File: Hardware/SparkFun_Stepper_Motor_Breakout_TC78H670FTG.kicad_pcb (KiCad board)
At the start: 4 copper layers, 15.2 x 20.3 mm, 45 parts, among them J1 Conn_01x08, J2 Conn_01x08, U1 TC78H670FTG

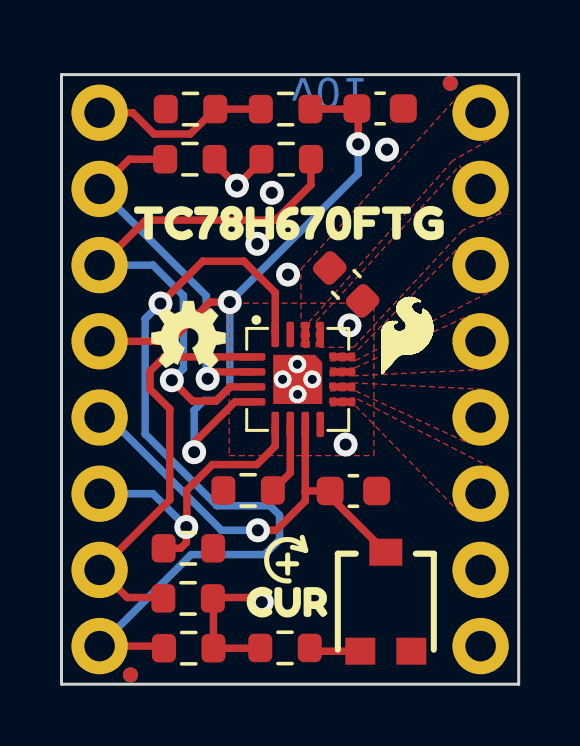
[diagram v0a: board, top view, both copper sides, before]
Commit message: more tweaks for DRC
-inner layer zone properties min width changed from .3 to .2 to allow flow and more thermal spokes on 3v3 header
-DRC exclusions for fiducials
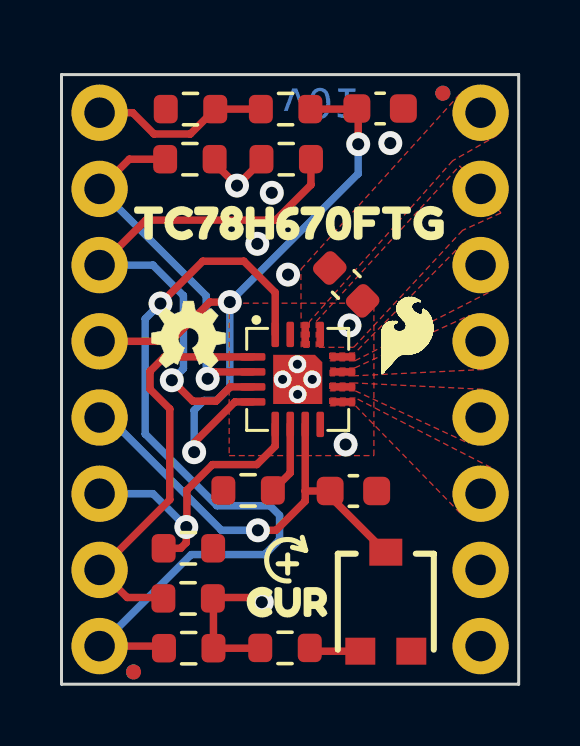
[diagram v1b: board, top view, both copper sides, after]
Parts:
- moved FID1 0.41 mm to (147.3, 94.6)
- moved FID2 0.41 mm to (147.3, 94.6)
- moved FID4 0.14 mm to (137.0, 113.9)
- moved FID3 0.14 mm to (137.0, 113.9)
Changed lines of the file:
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@@
     (property "Sheetfile" "SparkFun_Stepper_Motor_Carrier_TC78H670FTG.kicad_sch")
     (property "Sheetname" "")
-    (attr smd)
+    (attr smd allow_soldermask_bridges)
     (fp_text reference "U1" (at 0.75 -1.58 unlocked) (layer "F.Fab")
         (effects (font (size 1 1) (thickness 0.1)))
@@
   )
   (footprint "SparkFun-Aesthetic:Fiducial_0.5mm_Mask1mm" (layer "F.Cu")
-    (at 136.92 113.99)
+    (at 137.021639 113.891825)
     (descr "Circular Fiducial, 0.5mm bare copper, 1mm soldermask opening (Level C)")
     (tags "fiducial")
@@
   )
   (footprint "SparkFun-Aesthetic:Fiducial_0.5mm_Mask1mm" (layer "F.Cu")
-    (at 147.58 94.27)
+    (at 147.331908 94.601097)
     (descr "Circular Fiducial, 0.5mm bare copper, 1mm soldermask opening (Level C)")
     (tags "fiducial")
@@
   )
   (footprint "SparkFun-Aesthetic:Fiducial_0.5mm_Mask1mm" (layer "B.Cu")
-    (at 147.58 94.27 180)
+    (at 147.331908 94.599043 180)
     (descr "Circular Fiducial, 0.5mm bare copper, 1mm soldermask opening (Level C)")
     (tags "fiducial")
@@
   )
   (footprint "SparkFun-Aesthetic:Fiducial_0.5mm_Mask1mm" (layer "B.Cu")
-    (at 136.92 113.99 180)
+    (at 137.019585 113.89097 180)
     (descr "Circular Fiducial, 0.5mm bare copper, 1mm soldermask opening (Level C)")
     (tags "fiducial")
@@
   (gr_rect (start 134.62 93.98) (end 149.86 114.3)
     (stroke (width 0.1) (type default)) (fill none) (layer "Edge.Cuts"))
-  (gr_text "v01" (at 142.261552 93.973312 180) (layer "B.Cu")
+  (gr_text "v01" (at 141.988553 94.318209 180) (layer "B.Cu")
     (effects (font (size 1 1) (thickness 0.15)) (justify left bottom mirror))
   )
@@
   (via (at 141.296656 111.566922) (size 0.8) (drill 0.4) (layers "F.Cu" "B.Cu") (free) (net 8))
   (via (at 140.47 97.68) (size 0.8) (drill 0.4) (layers "F.Cu" "B.Cu") (free) (net 8))
-  (via (at 145.47 96.48) (size 0.8) (drill 0.4) (layers "F.Cu" "B.Cu") (net 13))
+  (via (at 145.579788 96.263383) (size 0.8) (drill 0.4) (layers "F.Cu" "B.Cu") (net 13))
   (via (at 141.1465 99.621194) (size 0.8) (drill 0.4) (layers "F.Cu" "B.Cu") (net 13))
   (via (at 141.99 104.14) (size 0.6) (drill 0.3) (layers "F.Cu" "B.Cu") (net 13))
@@
     (priority 6)
     (connect_pads (clearance 0.2032))
-    (min_thickness 0.3) (filled_areas_thickness no)
+    (min_thickness 0.2) (filled_areas_thickness no)
     (fill yes (thermal_gap 0.2032) (thermal_bridge_width 0.3))
     (polygon

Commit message: ordering instructions
Inner copper weight
Material: TG135
Four layer stack-up
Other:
- board text added: "0.5oz Inner Layers"
- board text added: "2oz Outer Layers"
- board text added: "JLC7628 Stackup"
- board text added: "Material: TG135-140"
- board text removed: "Copper weight: 2oz"
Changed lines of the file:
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@@
     (40 "Dwgs.User" user "User.Drawings")
     (41 "Cmts.User" user "User.Comments")
-    (42 "Eco1.User" user "Dimensions")
+    (42 "Eco1.User" user "Measures")
     (43 "Eco2.User" user "User.Eco2")
     (44 "Edge.Cuts" user)
@@
     (effects (font (size 2 2) (thickness 0.15)) (justify left bottom))
   )
+  (gr_text "JLC7628 Stackup" (at 170.18 88.9) (layer "F.Fab")
+    (effects (font (size 2 2) (thickness 0.15)) (justify left bottom))
+  )
+  (gr_text "2oz Outer Layers" (at 170.18 81.28) (layer "F.Fab")
+    (effects (font (size 2 2) (thickness 0.15)) (justify left bottom))
+  )
   (gr_text "Layers: 4" (at 170.27 73.31) (layer "F.Fab")
     (effects (font (size 2 2) (thickness 0.15)) (justify left bottom))
   )
+  (gr_text "Material: TG135-140" (at 170.18 86.36) (layer "F.Fab")
+    (effects (font (size 2 2) (thickness 0.15)) (justify left bottom))
+  )
   (gr_text "Thickness: 1.6mm" (at 170.18 78.74) (layer "F.Fab")
     (effects (font (size 2 2) (thickness 0.15)) (justify left bottom))
@@
     (effects (font (size 2 2) (thickness 0.15)) (justify left bottom))
   )
-  (gr_text "Copper weight: 2oz" (at 170.18 81.28) (layer "F.Fab")
+  (gr_text "0.5oz Inner Layers" (at 170.18 83.82) (layer "F.Fab")
     (effects (font (size 2 2) (thickness 0.15)) (justify left bottom))
   )
